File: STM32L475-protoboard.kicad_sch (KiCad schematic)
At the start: 63 parts, among them J1 USB_HEADER, J10 Conn_01x02_Male, J11 Conn_01x02_Male, J15 SD_Card, J2 USB_B_Micro, J3 DCin, J4 STLINK, J5 W5500_ETHERNET, J6 STLINK2, J7 BOOT_MODE, J9 Conn_02x16_Odd_Even, SW1 RESET, U1 SRV05-4, U2 AMS1117-3.3, U3 STM32L475RCTx, Y1 Crystal_GND24, Y2 32.768k

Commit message: some notes to schema
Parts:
- R3, R4: value 0 -> 22
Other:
- note added: "USB ID pin + pull-up datalinjaan tsekkaa DFU-homma A/D:t (LPF..) + DAC-linjat piikkiriman levennys"
- note added: "USB_OTG_FS_ID!!! TSEKKAA myös STM32 VBUS-pinni"
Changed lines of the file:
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@@
     (effects (font (size 1.27 1.27)) (justify left bottom))
+  )
+  (text "USB_OTG_FS_ID!!!\n\nTSEKKAA myös STM32 VBUS-pinni" (at 33.655 153.035 0)
+    (effects (font (size 2 2) (thickness 0.254) bold) (justify left bottom))
+  )
+  (text "USB ID pin + pull-up datalinjaan \ntsekkaa DFU-homma\n\nA/D:t (LPF..) + DAC-linjat\n\npiikkiriman levennys"
+    (at 156.21 17.78 0)
+    (effects (font (size 3 3) (thickness 0.6) bold) (justify left bottom))
   )
   (text "NC" (at 45.72 49.53 0)
@@
     (in_bom yes) (on_board yes)
     (property "Reference" "R4" (id 0) (at 187.96 69.85 90))
-    (property "Value" "0" (id 1) (at 187.96 72.39 90))
+    (property "Value" "22" (id 1) (at 187.96 72.39 90))
     (property "Footprint" "Resistor_SMD:R_0805_2012Metric_Pad1.20x1.40mm_HandSolder" (id 2) (at 187.96 74.93 0)
       (effects (font (size 1.27 1.27)) hide)
@@
     (in_bom yes) (on_board yes)
     (property "Reference" "R3" (id 0) (at 187.96 77.47 90))
-    (property "Value" "0" (id 1) (at 187.96 74.93 90))
+    (property "Value" "22" (id 1) (at 187.96 74.93 90))
     (property "Footprint" "Resistor_SMD:R_0805_2012Metric_Pad1.20x1.40mm_HandSolder" (id 2) (at 187.96 72.39 0)
       (effects (font (size 1.27 1.27)) hide)
@@
     )
     (path "/ccd3de7d-a21b-4960-85d4-260f1a0399f7"
-      (reference "R3") (unit 1) (value "0") (footprint "Resistor_SMD:R_0805_2012Metric_Pad1.20x1.40mm_HandSolder")
+      (reference "R3") (unit 1) (value "22") (footprint "Resistor_SMD:R_0805_2012Metric_Pad1.20x1.40mm_HandSolder")
     )
     (path "/2b5278ba-8374-4977-b726-bae867d1b2f1"
-      (reference "R4") (unit 1) (value "0") (footprint "Resistor_SMD:R_0805_2012Metric_Pad1.20x1.40mm_HandSolder")
+      (reference "R4") (unit 1) (value "22") (footprint "Resistor_SMD:R_0805_2012Metric_Pad1.20x1.40mm_HandSolder")
     )
     (path "/1f5a60c4-0b65-42e8-a7bb-f4f53a05b55c"

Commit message: save
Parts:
- added C5: 100u, Capacitor_SMD:C_0805_2012Metric_Pad1.18x1.45mm_HandSolder, symbol Device:C_Polarized
- added R5: 1.5k, Resistor_SMD:R_0603_1608Metric_Pad0.98x0.95mm_HandSolder, symbol Device:R_Small
- C4: value 220u -> 100u; footprint (none) -> Capacitor_SMD:C_0805_2012Metric_Pad1.18x1.45mm_HandSolder
- J8: renamed from J9; value Conn_02x16_Odd_Even -> Conn_02x20_Odd_Even; footprint Connector_PinHeader_2.54mm:PinHeader_2x16_P2.54mm_Vertical -> Connector_PinHeader_2.54mm:PinHeader_2x20_P2.54mm_Vertical; symbol Connector_Generic:Conn_02x16_Odd_Even -> Connector_Generic:Conn_02x20_Odd_Even
- R1: footprint Resistor_SMD:R_0603_1608Metric -> Resistor_SMD:R_0603_1608Metric_Pad0.98x0.95mm_HandSolder
- R3, R4: footprint Resistor_SMD:R_0805_2012Metric_Pad1.20x1.40mm_HandSolder -> Resistor_SMD:R_0603_1608Metric_Pad0.98x0.95mm_HandSolder
- R6: renamed from R5; footprint Resistor_SMD:R_0805_2012Metric_Pad1.20x1.40mm_HandSolder -> Resistor_SMD:R_0603_1608Metric_Pad0.98x0.95mm_HandSolder
- R7: renamed from R6; footprint Resistor_SMD:R_0805_2012Metric_Pad1.20x1.40mm_HandSolder -> Resistor_SMD:R_0603_1608Metric_Pad0.98x0.95mm_HandSolder
- renumbered C8 to C10, C9 to C11, C10 to C12, C11 to C13, C12 to C14, C13 to C15, C14 to C16, C15 to C17, C16 to C18, C18 to C19, C19 to C20, C20 to C21, C5 to C6, C17 to C7, C6 to C8, C7 to C9, J11 to J10, J15 to J11, J10 to J9, R9 to R10, R10 to R11, R11 to R12, R7 to R8, R8 to R9
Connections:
- net +3V3: now also J8.5 (Pin_5), R5.2; no longer J8.1 (Pin_1)
- net GND: now also J8.34 (Pin_34), J8.36 (Pin_36), J8.38 (Pin_38), J8.40 (Pin_40), C5.2
- net USB_D+: now also R5.1
- net VBUS: now also J8.3 (Pin_3)
- net at C3.1, C4.1, C6.1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: now also C5.1
- net USB_ID: now reaches U3.43 (PA10)
- net USB_ID: now also J2.4 (ID)
- net +VDC: now reaches C1.1, D1.2 (A), F2.1
- net +VDC: now also J8.1 (Pin_1)
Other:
- note removed: "100u kerkot (basic)"
- moved on the sheet: C6

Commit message: saveä
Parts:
- added H5: MountingHole_Pad, MountingHole:MountingHole_2.2mm_M2_DIN965_Pad_TopBottom, symbol Mechanical:MountingHole_Pad
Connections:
- net LED_USR1: now also J8.37 (Pin_37)
- net LED_USR2: now reaches U3.15 (PA1)
- net LED_USR2: now also J8.39 (Pin_39), R7.1
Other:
- moved on the sheet: J8

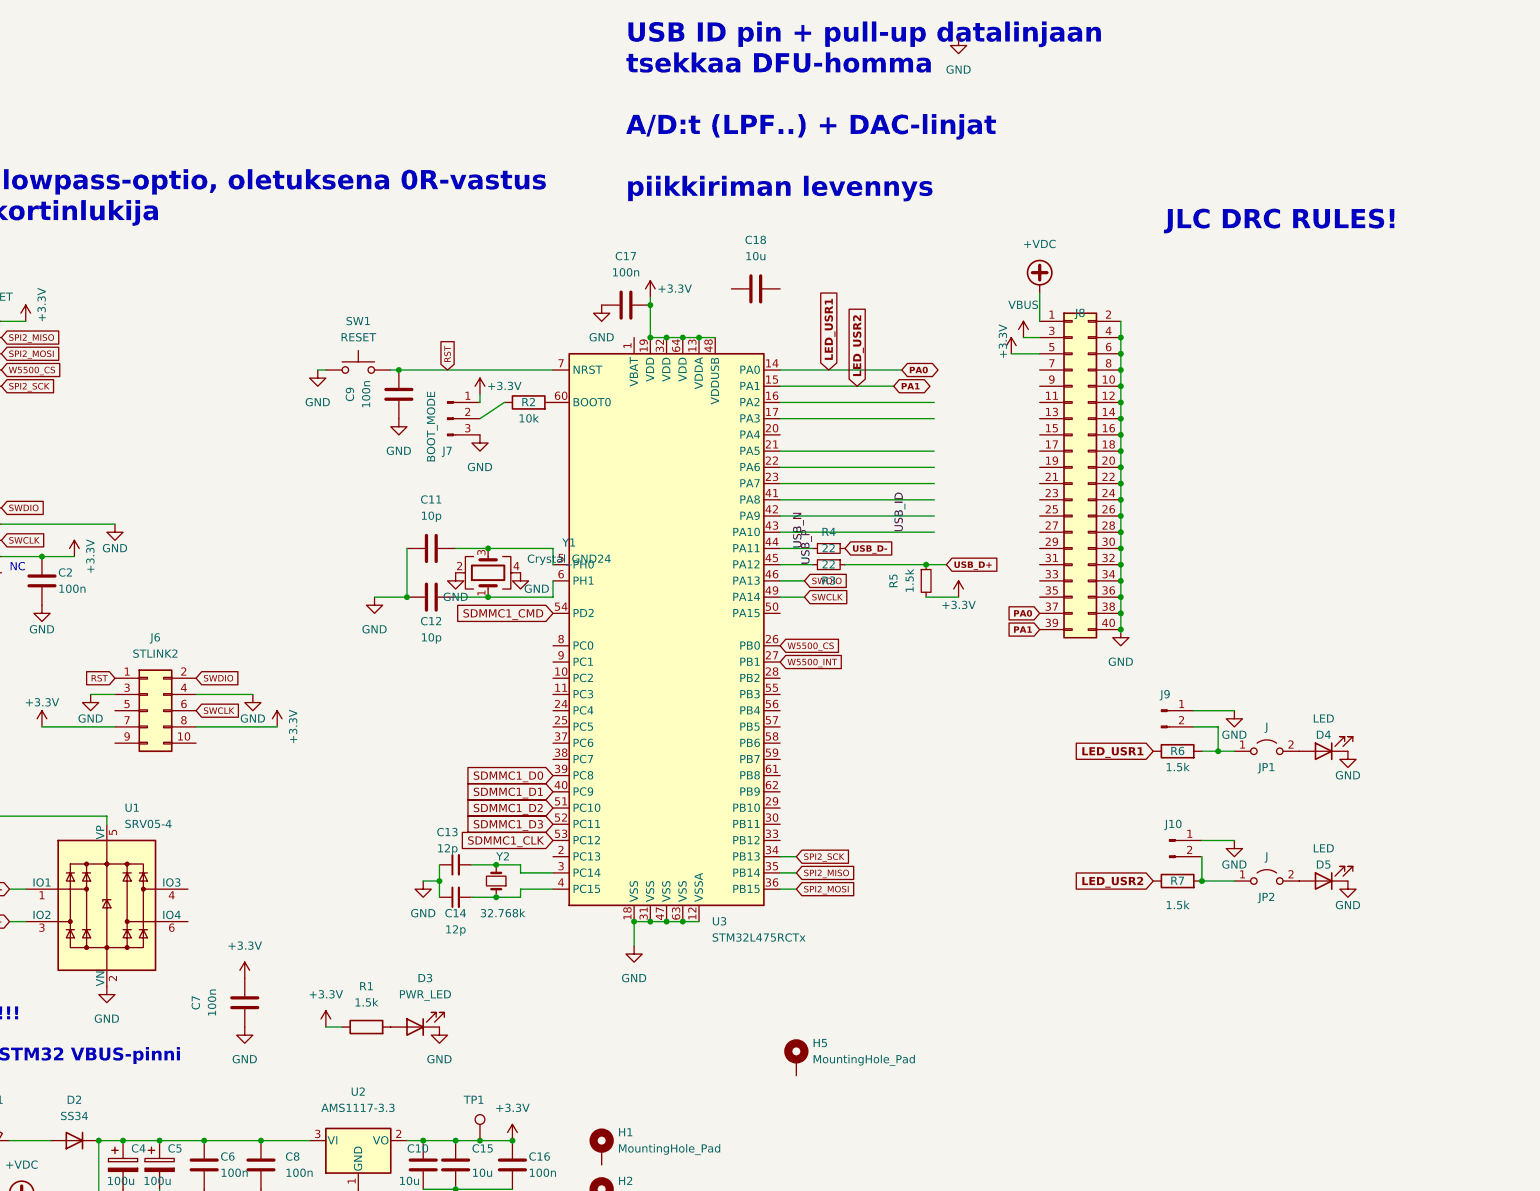
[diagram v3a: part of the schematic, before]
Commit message: STM32L475 should have internal pullup for USB line, but need to be checked (now DNP resistor)
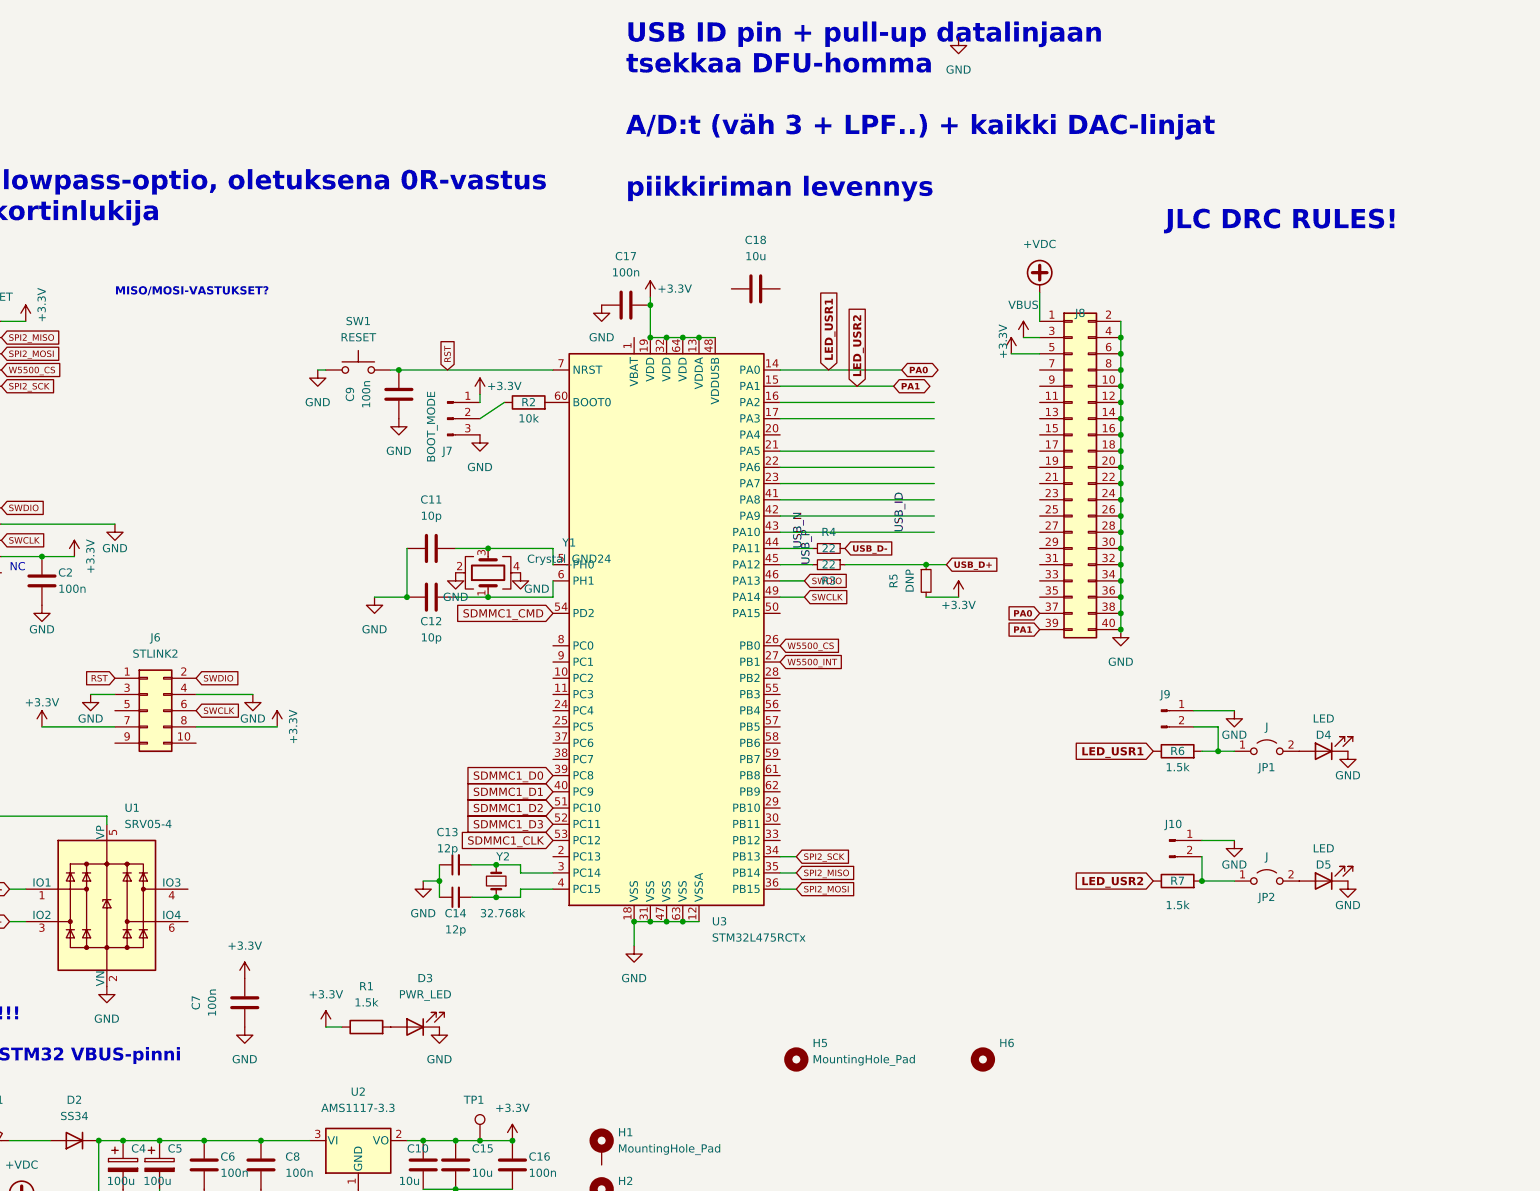
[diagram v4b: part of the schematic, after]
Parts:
- added H6: MountingHole_Pad, MountingHole:MountingHole_2.2mm_M2_DIN965_Pad_TopBottom, symbol Mechanical:MountingHole
- H5: symbol Mechanical:MountingHole_Pad -> Mechanical:MountingHole
- R5: value 1.5k -> DNP
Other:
- note added: "MISO/MOSI-VASTUKSET?"
- note added: "USB ID pin + pull-up datalinjaan tsekkaa DFU-homma A/D:t (väh 3 + LPF..) + kaikki DAC-linjat piikkiriman levennys"
- note removed: "USB ID pin + pull-up datalinjaan tsekkaa DFU-homma A/D:t (LPF..) + DAC-linjat piikkiriman levennys"
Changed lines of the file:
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@@
     (effects (font (size 2 2) (thickness 0.254) bold) (justify left bottom))
   )
-  (text "USB ID pin + pull-up datalinjaan \ntsekkaa DFU-homma\n\nA/D:t (LPF..) + DAC-linjat\n\npiikkiriman levennys"
+  (text "USB ID pin + pull-up datalinjaan \ntsekkaa DFU-homma\n\nA/D:t (väh 3 + LPF..) + kaikki DAC-linjat\n\npiikkiriman levennys"
     (at 156.21 17.78 0)
     (effects (font (size 3 3) (thickness 0.6) bold) (justify left bottom))
@@
   (text "NC" (at 45.72 49.53 0)
     (effects (font (size 1 1) (thickness 0.2) bold) (justify left bottom))
+  )
+  (text "MISO/MOSI-VASTUKSET?" (at 76.2 33.02 0)
+    (effects (font (size 1.27 1.27) (thickness 0.254) bold) (justify left bottom))
   )
   (text "NC" (at 59.69 76.2 0)
@@
     (pin "1")
   )
-  (symbol (lib_id "Mechanical:MountingHole_Pad") (at 182.88 152.4 0) (unit 1)
+  (symbol (lib_id "Mechanical:MountingHole") (at 182.88 152.4 0) (unit 1)
     (in_bom yes) (on_board yes) (fields_autoplaced)
     (property "Reference" "H5" (id 0) (at 185.42 149.8599 0)
@@
       (effects (font (size 1.27 1.27)) hide)
     )
-    (pin "1")
   )
   (symbol (lib_id "power:+3.3V") (at 133.35 48.26 0) (unit 1)
@@
     (in_bom yes) (on_board yes)
     (property "Reference" "R5" (id 0) (at 198.12 77.47 90))
-    (property "Value" "1.5k" (id 1) (at 200.66 77.47 90))
+    (property "Value" "DNP" (id 1) (at 200.66 77.47 90))
     (property "Footprint" "Resistor_SMD:R_0603_1608Metric_Pad0.98x0.95mm_HandSolder" (id 2) (at 203.2 77.47 0)
       (effects (font (size 1.27 1.27)) hide)
@@
     (pin "1")
     (pin "2")
+  )
+  (symbol (lib_id "Mechanical:MountingHole") (at 212.09 152.4 0) (unit 1)
+    (in_bom yes) (on_board yes) (fields_autoplaced)
+    (property "Reference" "H6" (id 0) (at 214.63 149.8599 0)
+      (effects (font (size 1.27 1.27)) (justify left))
+    )
+    (property "Value" "MountingHole_Pad" (id 1) (at 214.63 152.3999 0)
+      (effects (font (size 1.27 1.27)) (justify left) hide)
+    )
+    (property "Footprint" "MountingHole:MountingHole_2.2mm_M2_DIN965_Pad_TopBottom" (id 2) (at 212.09 152.4 0)
+      (effects (font (size 1.27 1.27)) hide)
+    )
+    (property "Datasheet" "~" (id 3) (at 212.09 152.4 0)
+      (effects (font (size 1.27 1.27)) hide)
+    )
   )
   (symbol (lib_id "Device:C") (at 337.82 144.78 180) (unit 1)
@@
       (reference "H5") (unit 1) (value "MountingHole_Pad") (footprint "MountingHole:MountingHole_2.2mm_M2_DIN965_Pad_TopBottom")
     )
+    (path "/befd4089-387e-42a9-a623-d2d12dac6ec5"
+      (reference "H6") (unit 1) (value "MountingHole_Pad") (footprint "MountingHole:MountingHole_2.2mm_M2_DIN965_Pad_TopBottom")
+    )
     (path "/2bee3e87-6d07-45df-9bcd-92a8c3fbdbce"
       (reference "J1") (unit 1) (value "USB_HEADER") (footprint "Connector_PinHeader_2.54mm:PinHeader_1x04_P2.54mm_Vertical")
@@
     )
     (path "/b459df84-9128-4384-901e-fea7f60b4c50"
-      (reference "R5") (unit 1) (value "1.5k") (footprint "Resistor_SMD:R_0603_1608Metric_Pad0.98x0.95mm_HandSolder")
+      (reference "R5") (unit 1) (value "DNP") (footprint "Resistor_SMD:R_0603_1608Metric_Pad0.98x0.95mm_HandSolder")
     )
     (path "/1f5a60c4-0b65-42e8-a7bb-f4f53a05b55c"

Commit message: todo update
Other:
- note added: "TODO: A/D:lle lowpass-optio, oletuksena 0R-vastus"
- note added: "USB ID pin + pull-up datalinjaan tsekkaa DFU-homma A/D:t (väh 3 + LPF..) + kaikki DAC-linjat"
- note removed: "TODO: A/D:lle lowpass-optio, oletuksena 0R-vastus SD/MICROSD-kortinlukija"
- note removed: "USB ID pin + pull-up datalinjaan tsekkaa DFU-homma A/D:t (väh 3 + LPF..) + kaikki DAC-linjat piikkiriman levennys"
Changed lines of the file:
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@@
     (stroke (width 0) (type default) (color 0 0 0 0))
   )
-  (text "JLC DRC RULES!" (at 240.665 22.86 0)
+  (text "JLC DRC RULES!" (at 241.3 29.21 0)
     (effects (font (size 3 3) (thickness 0.6) bold) (justify left bottom))
   )
@@
     (effects (font (size 2 2) (thickness 0.254) bold) (justify left bottom))
   )
-  (text "USB ID pin + pull-up datalinjaan \ntsekkaa DFU-homma\n\nA/D:t (väh 3 + LPF..) + kaikki DAC-linjat\n\npiikkiriman levennys"
+  (text "USB ID pin + pull-up datalinjaan \ntsekkaa DFU-homma\n\nA/D:t (väh 3 + LPF..) + kaikki DAC-linjat\n"
     (at 156.21 17.78 0)
     (effects (font (size 3 3) (thickness 0.6) bold) (justify left bottom))
@@
     (effects (font (size 1.27 1.27)) (justify left bottom))
   )
-  (text "TODO: A/D:lle lowpass-optio, oletuksena 0R-vastus\nSD/MICROSD-kortinlukija"
-    (at 25.4 21.59 0)
+  (text "TODO: A/D:lle lowpass-optio, \noletuksena 0R-vastus"
+    (at 72.39 24.13 0)
     (effects (font (size 3 3) (thickness 0.6) bold) (justify left bottom))
   )

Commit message: layout
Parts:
- added C9: 10p, Capacitor_SMD:C_0603_1608Metric, symbol Device:C
- added R1: 1k, Resistor_SMD:R_0603_1608Metric_Pad0.98x0.95mm_HandSolder, symbol Device:R
- renumbered C9 to C10, C10 to C11, C11 to C12, C12 to C13, C13 to C14, C14 to C15, C15 to C16, C16 to C17, C17 to C18, C18 to C19, C19 to C20, C20 to C21, C21 to C22, R9 to R10, R10 to R11, R11 to R12, R12 to R13, R1 to R2, R2 to R3, R3 to R4, R4 to R5, R5 to R6, R6 to R7, R7 to R8, R8 to R9
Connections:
- net GND: now also C9.2
- net RST: now also R1.2; no longer SW1.2
- new net: C9.1, R1.1, SW1.2
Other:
- moved on the sheet: SW1

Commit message: some fixes
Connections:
- net +3V3: now also J7.3 (Pin_3); no longer J7.1 (Pin_1)
- net GND: now also J7.1 (Pin_1); no longer J7.3 (Pin_3)
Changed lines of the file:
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@@
     (pin "2")
   )
-  (symbol (lib_id "Connector:Conn_01x03_Male") (at 128.27 52.07 0) (unit 1)
+  (symbol (lib_id "Connector:Conn_01x03_Male") (at 128.27 52.07 0) (mirror x) (unit 1)
     (in_bom yes) (on_board yes)
-    (property "Reference" "J7" (id 0) (at 128.27 57.15 0))
-    (property "Value" "BOOT_MODE" (id 1) (at 125.73 53.34 90))
+    (property "Reference" "J7" (id 0) (at 128.27 46.99 0))
+    (property "Value" "BOOT_MODE" (id 1) (at 125.73 50.8 90))
     (property "Footprint" "Connector_PinHeader_2.54mm:PinHeader_1x03_P2.54mm_Vertical" (id 2) (at 128.27 52.07 0)
       (effects (font (size 1.27 1.27)) hide)

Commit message: some routing
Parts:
- C1, C4, C5: value 100u -> 22u; LCSC (none) -> C45783
- C11, C19: value 10u -> 22u; LCSC (none) -> C45783
- C16: value 10u -> 100n
- C20, C21: LCSC (none) -> C45783
- U1: LCSC (none) -> C85364
- U2: LCSC (none) -> C6186
- Y1: value Crystal_GND24 -> 16 MHz; LCSC (none) -> C13738
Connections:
- net +3V3: now also C19.2
- net GND: now also C19.1
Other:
- moved on the sheet: C19, C7, D3, R2
